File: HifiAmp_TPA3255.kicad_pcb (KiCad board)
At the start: 4 copper layers, 200 x 150 mm, 124 parts, among them J1 PVDD 48V IN — NEEDS_DATA, J2 RCA L SE, J3 RCA R SE, J301 SPK_L, J302 SPK_R, J4 VOLUME_REMOTE, Q301 IPP330P10NM, Q302 IXTK200N10L2, U1 LM5010ASD, U2 LM2940IMP-12/NOPB, U3 TLV1117-33IDCY, U4 OPA1612AIDR, U5 OPA1612AIDR, U6 TPA3255B, U7 TPS3802K33DCKR, U8 LM5069-2

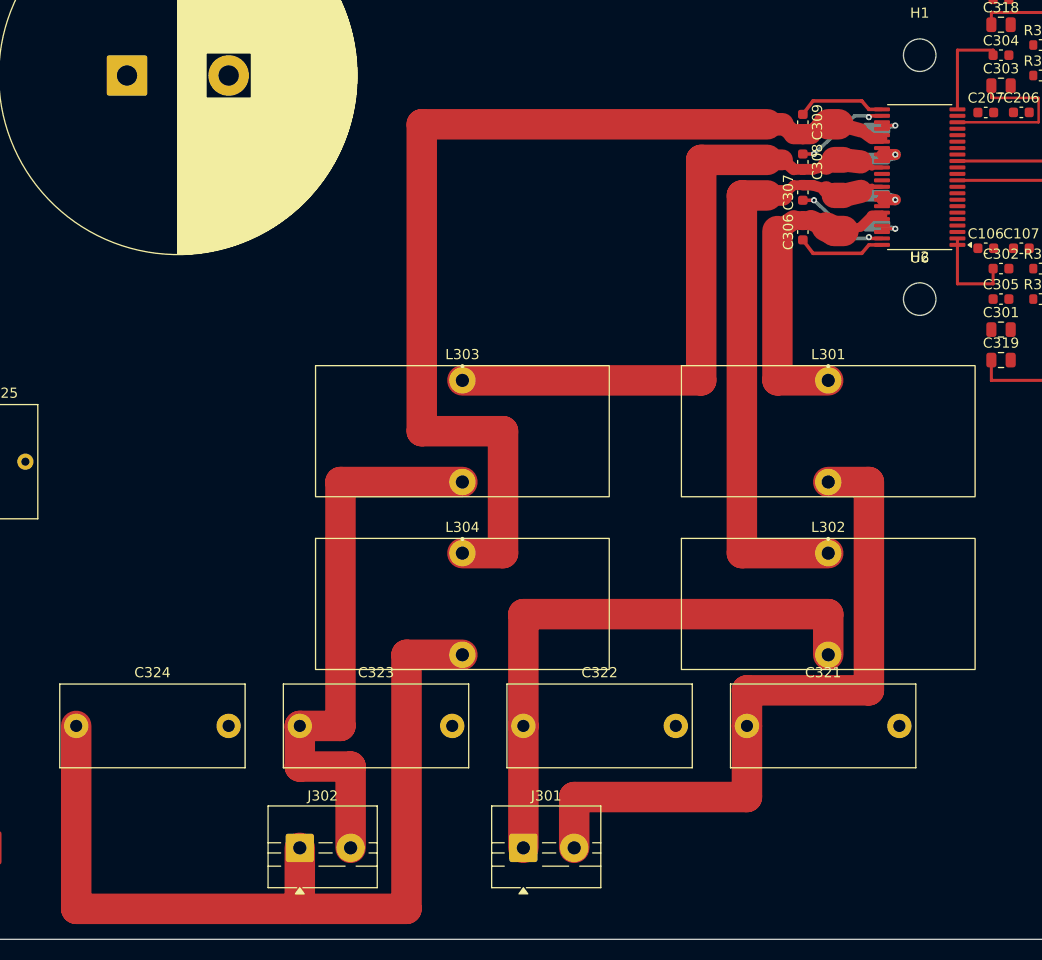
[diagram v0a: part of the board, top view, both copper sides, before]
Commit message: feat(f1.2-c2): apply the staggered-brick output placement, reroute the stage
The four toroids and the four bootstraps move to option O1 (C306 at 180 deg
so its BST pad clears the OUT_A vertical); OUT_x, OUT_x_F and BST_A..D are
rerouted, all OUT copper on F.Cu without vias.

Bridge pairs now match: A/B 29.13/28.92 mm, C/D 68.27/71.89 mm (OUT_D was
101 mm). Widths below 3.00 mm remain only at x >= 277.2, in U6's fine
pitch and around its BST vias; every OUT_x_F is 3.00 mm. DRC clean,
unconnected 216, parity 3, 124 footprints, 119 (units. The U6 escape rule
is still selective: 11 clearance errors without it, all on U6. Closes F1.2.

Co-Authored-By: Claude Opus 5.5 <noreply@anthropic.com>
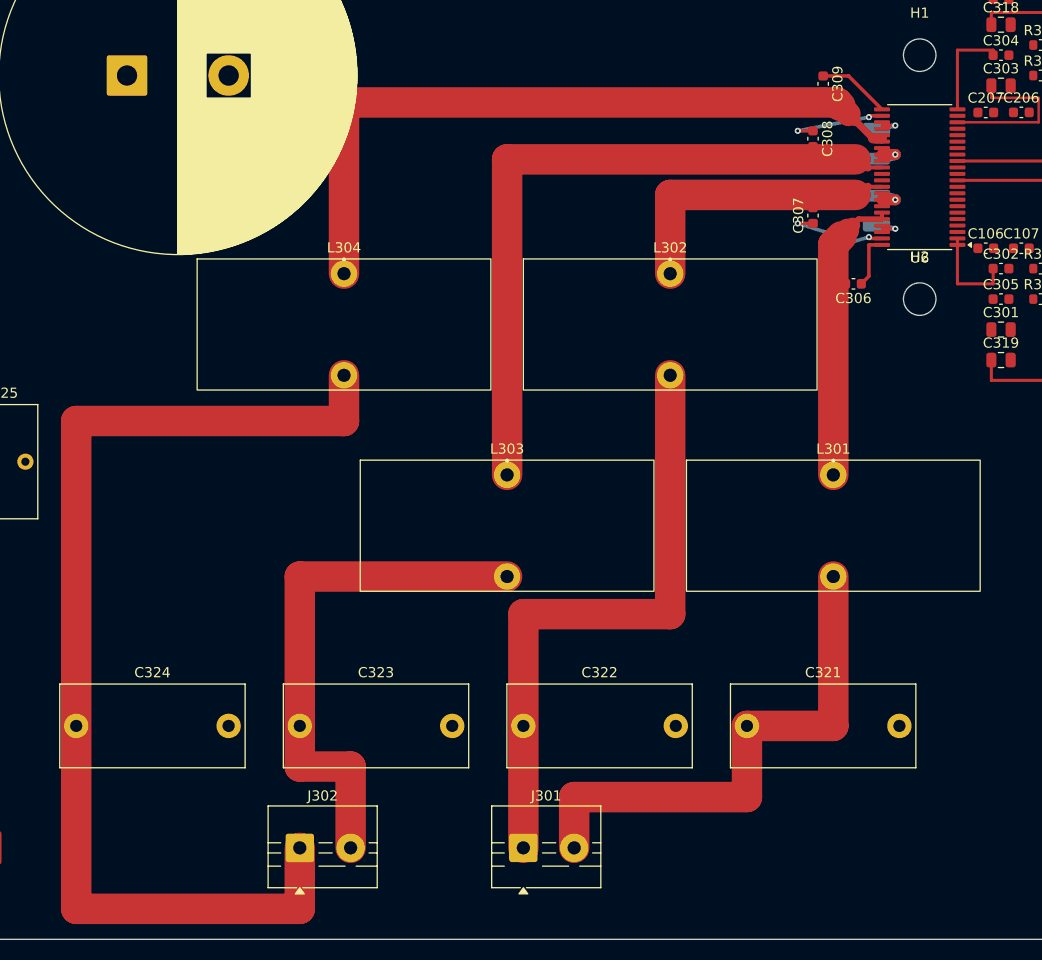
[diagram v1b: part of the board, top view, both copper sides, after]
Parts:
- moved L302 31.6 mm to (260.4, 184.5)
- moved L304 29.9 mm to (228.3, 184.5)
- moved L303 10.3 mm to (244.4, 204.3)
- moved L301 9.31 mm to (276.5, 204.3)
- moved C306 7.13 mm to (278.5, 185.5), turned to 180 degrees
- moved C309 4.28 mm to (275.5, 165.8)
- moved C307 2.49 mm to (274.5, 178.8)
- moved C308 2.49 mm to (274.5, 171.2)
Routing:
- net /OUT_B: track 58.3 -> 28.9 mm
- net /OUT_D: track 101.2 -> 71.9 mm
- net /OUT_D_F: track 87.0 -> 106.8 mm
- net /OUT_A_F: track 69.0 -> 52.2 mm
- net /OUT_C_F: track 57.0 -> 52.1 mm
- net /OUT_C: track 63.7 -> 68.3 mm
- net /OUT_B_F: track 57.0 -> 60.9 mm
- net /BST_A: track 8.84 -> 5.43 mm
- net /OUT_A: track 31.7 -> 29.1 mm
- net /BST_D: track 8.84 -> 7.15 mm
- net /BST_B: track 9.28 -> 10.1 mm
- net /BST_C: track 9.28 -> 9.92 mm

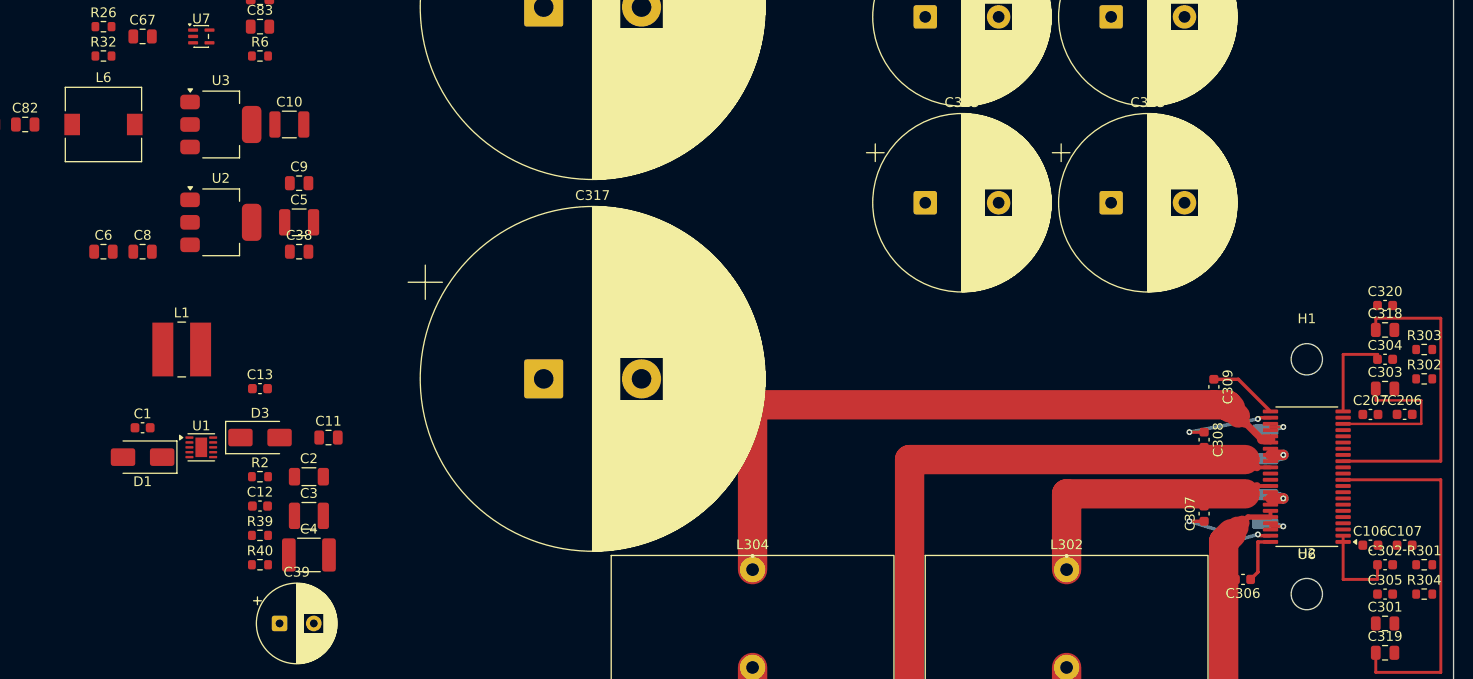
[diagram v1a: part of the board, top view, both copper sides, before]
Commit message: feat(f1.3-a): route the auxiliary buck U1 and the +12V/+15V/+3V3 rails
Hot loop first, FB away from SW, VCC/BST hop to B.Cu. Unconnected 216 -> 186,
DRC silk-only, parity 3. Opens F1.6 for the missing BUCK_VIN decoupling.

Co-Authored-By: Claude Opus 5.5 <noreply@anthropic.com>
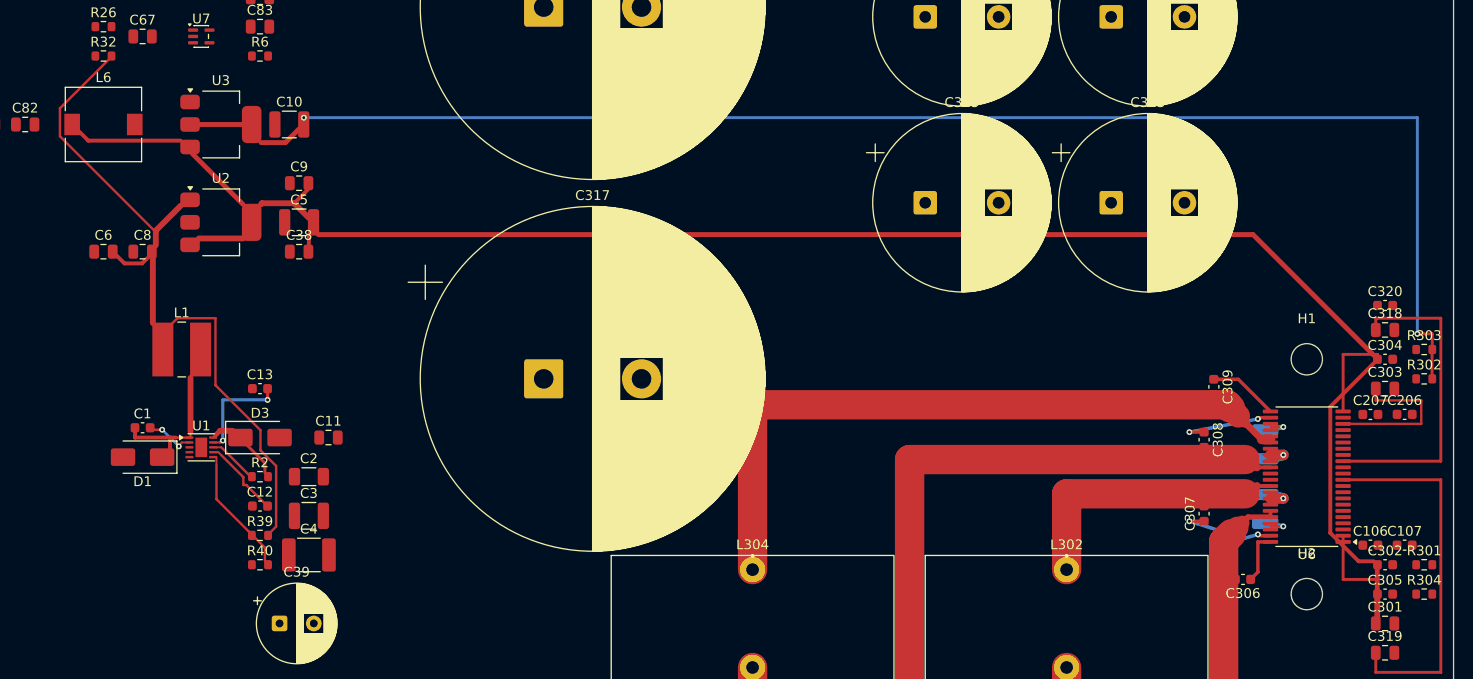
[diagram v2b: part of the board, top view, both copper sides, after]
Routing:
- net /+12V: track 19.3 -> 192.5 mm
- net /+3V3: track 0.00 -> 150.2 mm, vias 0 -> 2
- net /+15V: track 0.00 -> 68.3 mm
- net /SW: track 0.00 -> 14.0 mm
- net /FB: track 0.00 -> 12.6 mm
- net /VCC: track 0.00 -> 10.9 mm, vias 0 -> 2
- net /BUCK_VIN: track 0.00 -> 7.94 mm
- net /SS: track 0.00 -> 7.45 mm
- net /BST: track 0.00 -> 4.59 mm, vias 0 -> 2
- net /RON_SD: track 0.00 -> 4.46 mm

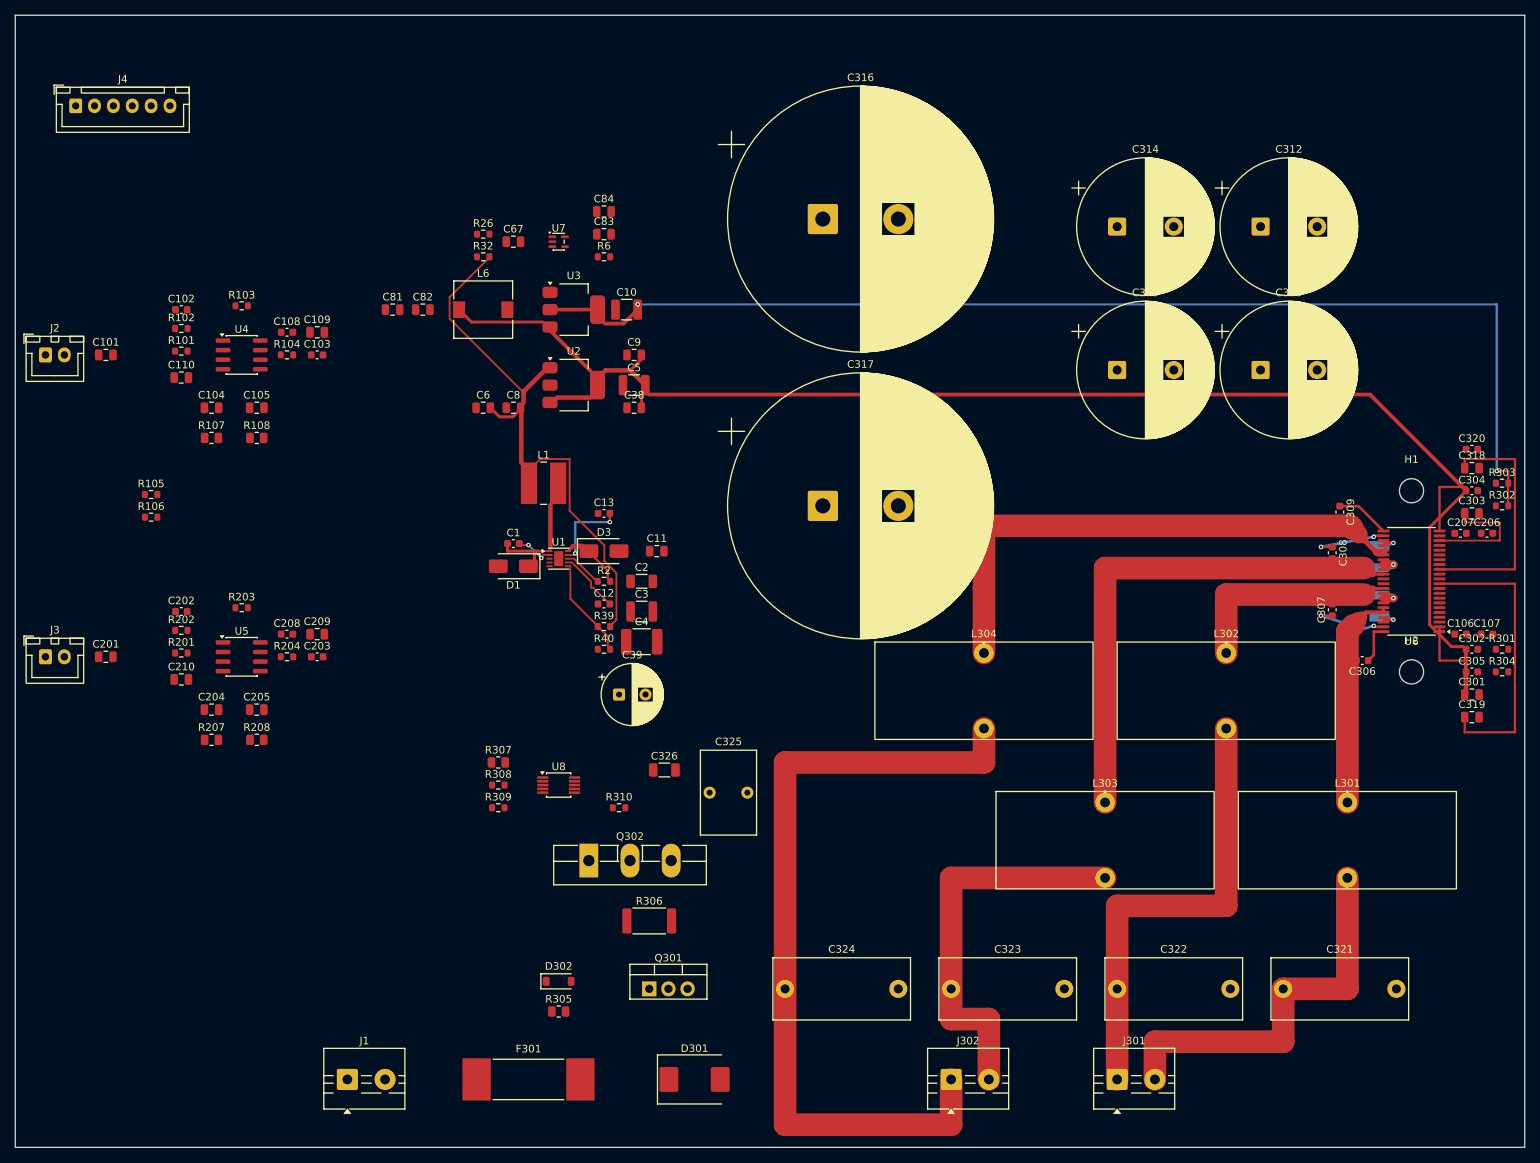
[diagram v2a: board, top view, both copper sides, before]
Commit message: feat(f1.3-b): route the power entry, LM5069 protection and ISEN
Power path sized to 4.95 A nominal (up to 7 mm on B.Cu), Kelvin sense on
R306, Q301 drain area kept free for F1.4. Selective 0.15 mm escape rules for
U8 and U1. Unconnected 186 -> 147, DRC silk-only, parity 3.

Co-Authored-By: Claude Opus 5.5 <noreply@anthropic.com>
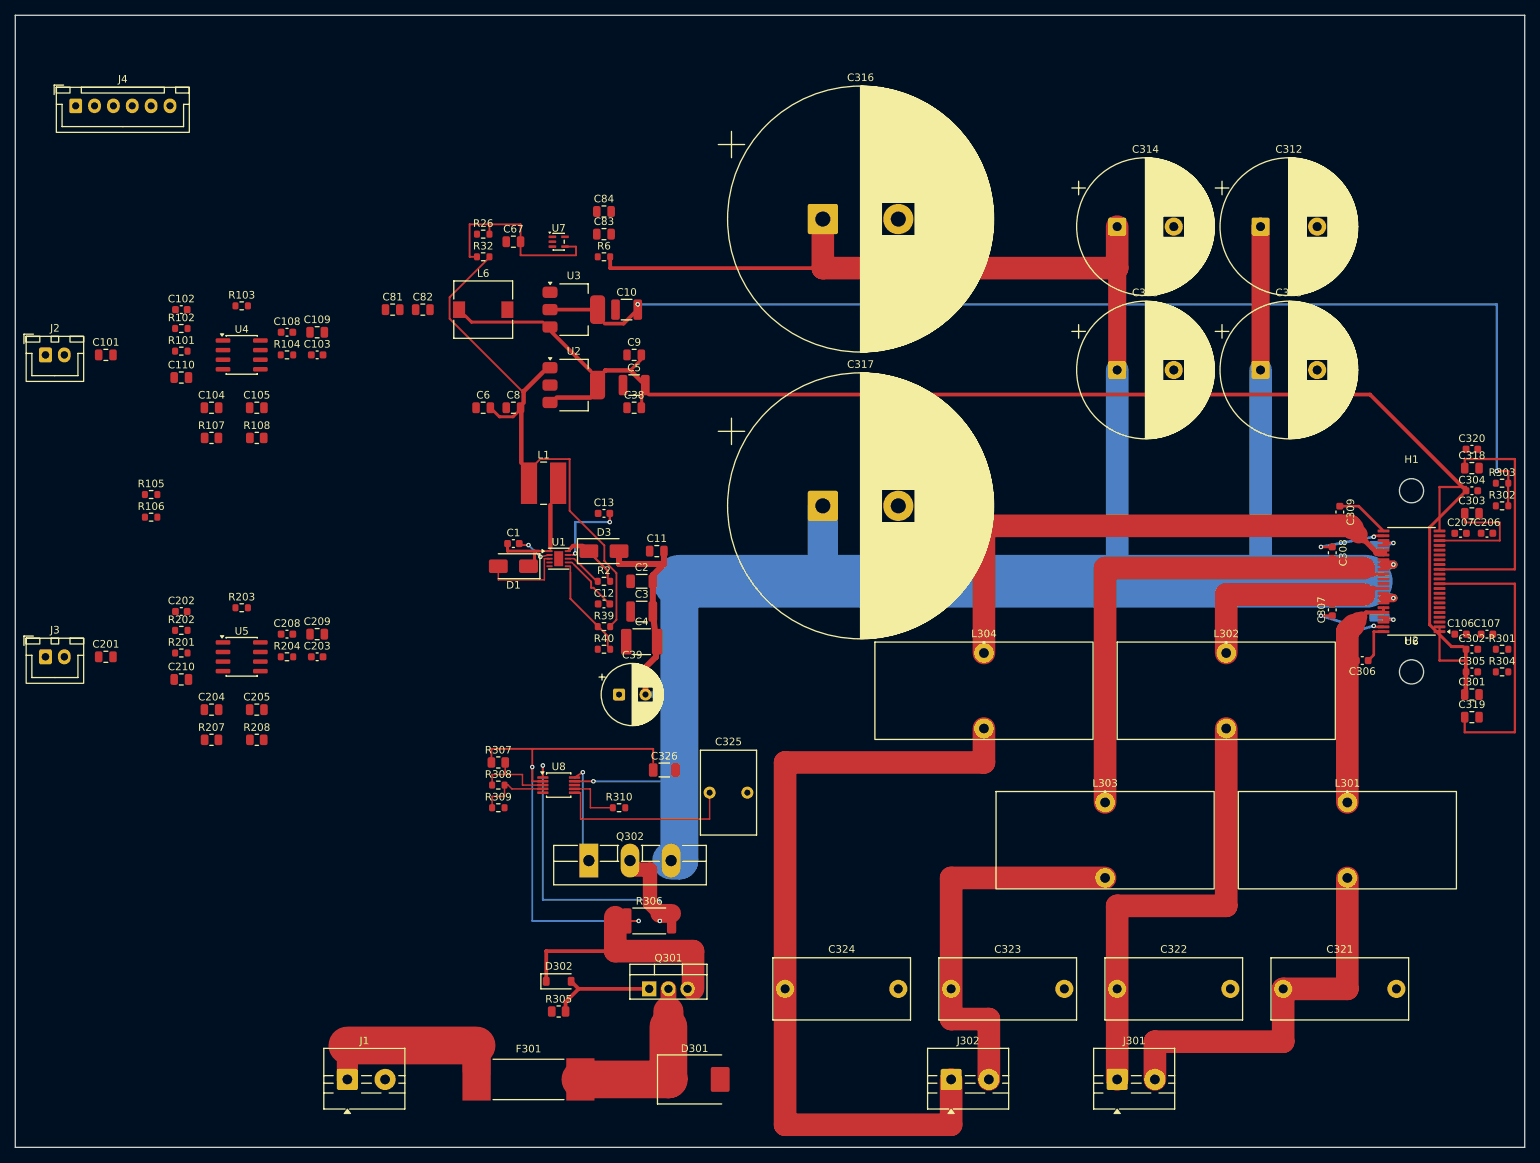
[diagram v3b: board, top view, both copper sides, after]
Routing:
- net /PVDD: track 6.41 -> 362.9 mm, vias 2 -> 3
- net /PVDD_PROT: track 0.00 -> 99.3 mm, vias 0 -> 2
- net /PVDD_SENSE: track 0.00 -> 48.8 mm, vias 0 -> 2
- net /VSENSE: track 0.00 -> 27.4 mm
- net /PVDD_EXT: track 0.00 -> 25.1 mm
- net /LM5069_TIMER: track 0.00 -> 24.9 mm
- net /PVDD_FUSED: track 0.00 -> 23.7 mm
- net /Q301_GATE: track 0.00 -> 14.5 mm
- net /HS_GATE: track 0.00 -> 11.5 mm, vias 0 -> 1
- net /ISEN: track 0.00 -> 11.4 mm
- net /LM5069_UVLO: track 0.00 -> 11.1 mm
- net /LM5069_OVLO: track 0.00 -> 9.93 mm
- net /LM5069_PWR: track 0.00 -> 7.58 mm
